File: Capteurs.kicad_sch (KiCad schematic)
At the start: 5 parts, among them U1 BME280

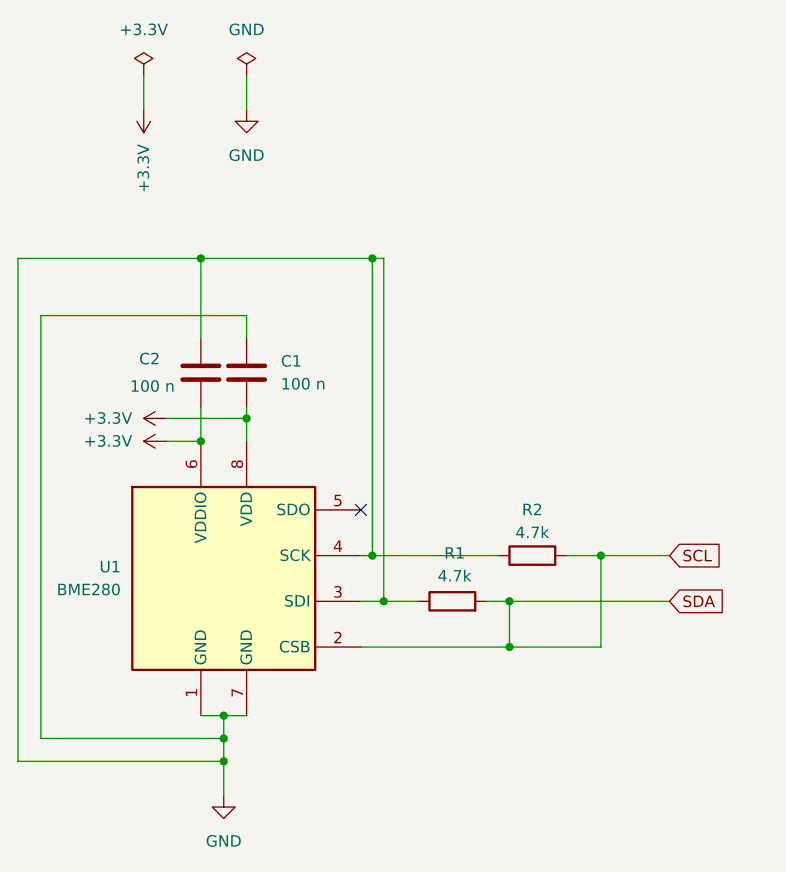
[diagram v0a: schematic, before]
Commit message: Correction capteur + ajout composant
Il fallait changer le nom dans le gestionnaire de footprint
Correction de la connectique du capteur, mais à vérifier quand même
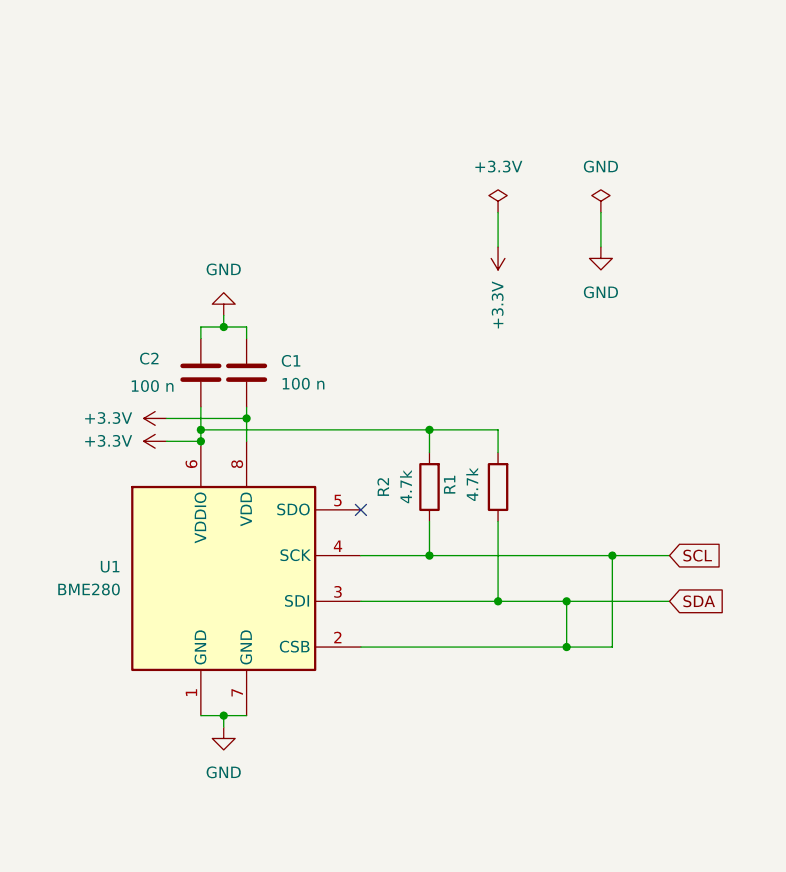
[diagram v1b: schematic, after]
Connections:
- net +3.3V: now also R1.2, R2.2
- net GND: no longer R1.1, R2.1, U1.3 (SDI), U1.4 (SCK)
- net SCL: now also R1.1, R2.1, U1.3 (SDI), U1.4 (SCK); no longer R1.2, R2.2
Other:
- moved on the sheet: R1, R2

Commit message: Dernieres pour review
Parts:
- removed R1, R2: 4.7k, symbol Device:R
- added R1, R2: 4k7, symbol Device:R_Small
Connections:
- net +3.3V: now also U1.2 (CSB), R1.2, R2.1
- net SCL: now also R1.1; no longer U1.2 (CSB), U1.3 (SDI)
- new net SDA: R2.2, U1.3 (SDI)

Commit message: revue schema
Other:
- note added: "SDO à la masse"
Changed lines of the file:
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@@
 	(generator_version "9.0")
 	(paper "A4")
+	(text "SDO à la masse\n"
+		(exclude_from_sim no)
+		(at 166.878 84.582 0)
+		(effects
+			(font
+				(size 1.27 1.27)
+				(color 255 0 0 1)
+			)
+		)
+	)
 	(junction
 		(at 137.16 77.47)

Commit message: premieres modif depuis la review
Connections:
- net GND: now also U1.5 (SDO)
- no-connect marks 1 -> 0
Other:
- note removed: "SDO à la masse"
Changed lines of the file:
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@@
 	(generator_version "9.0")
 	(paper "A4")
-	(text "SDO à la masse\n"
-		(exclude_from_sim no)
-		(at 166.878 84.582 0)
-		(effects
-			(font
-				(size 1.27 1.27)
-				(color 255 0 0 1)
-			)
-		)
-	)
 	(junction
 		(at 137.16 77.47)
@@
 		(color 0 0 0 0)
 	)
-	(no_connect
-		(at 154.94 85.09)
-	)
 	(wire
 		(pts
@@
 		(pts
 			(xy 137.16 64.77) (xy 139.7 64.77)
+		)
+		(stroke
+			(width 0)
+			(type default)
+		)
+	)
+	(wire
+		(pts
+			(xy 154.94 85.09) (xy 158.75 85.09)
 		)
 		(stroke
@@
 					(unit 1)
 				)
+			)
+		)
+	)
+	(symbol
+		(lib_id "power:GND")
+		(at 158.75 85.09 90)
+		(unit 1)
+		(exclude_from_sim no)
+		(in_bom yes)
+		(on_board yes)
+		(dnp no)
+		(fields_autoplaced yes)
+		(property "Reference" "#PWR023"
+			(at 165.1 85.09 0)
+			(effects
+				(font
+					(size 1.27 1.27)
+				)
+				(hide yes)
+			)
+		)
+		(property "Value" "GND"
+			(at 162.56 85.0899 90)
+			(effects
+				(font
+					(size 1.27 1.27)
+				)
+				(justify right)
+			)
+		)
+		(property "Footprint" ""
+			(at 158.75 85.09 0)
+			(effects
+				(font
+					(size 1.27 1.27)
+				)
+				(hide yes)
+			)
+		)
+		(property "Datasheet" ""
+			(at 158.75 85.09 0)
+			(effects
+				(font
+					(size 1.27 1.27)
+				)
+				(hide yes)
+			)
+		)
+		(property "Description" "Power symbol creates a global label with name \"GND\" , ground"
+			(at 158.75 85.09 0)
+			(effects
+				(font
+					(size 1.27 1.27)
+				)
+				(hide yes)
+			)
+		)
+		(pin "1"
+		)
+		(instances
+			(project ""
+				(path "/90bd0b60-6e70-43e1-8410-99fb54688c17/d62bceb2-9908-4d7c-aad2-bbefb30f6285"
+					(reference "#PWR023")
+					(unit 1)
+				)
